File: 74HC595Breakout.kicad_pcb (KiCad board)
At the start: 2 copper layers, 30.7 x 33.5 mm, 12 parts, among them J1 Input, J2 Chain, J3 Output, U1 74HC595, U2 ULN2803A

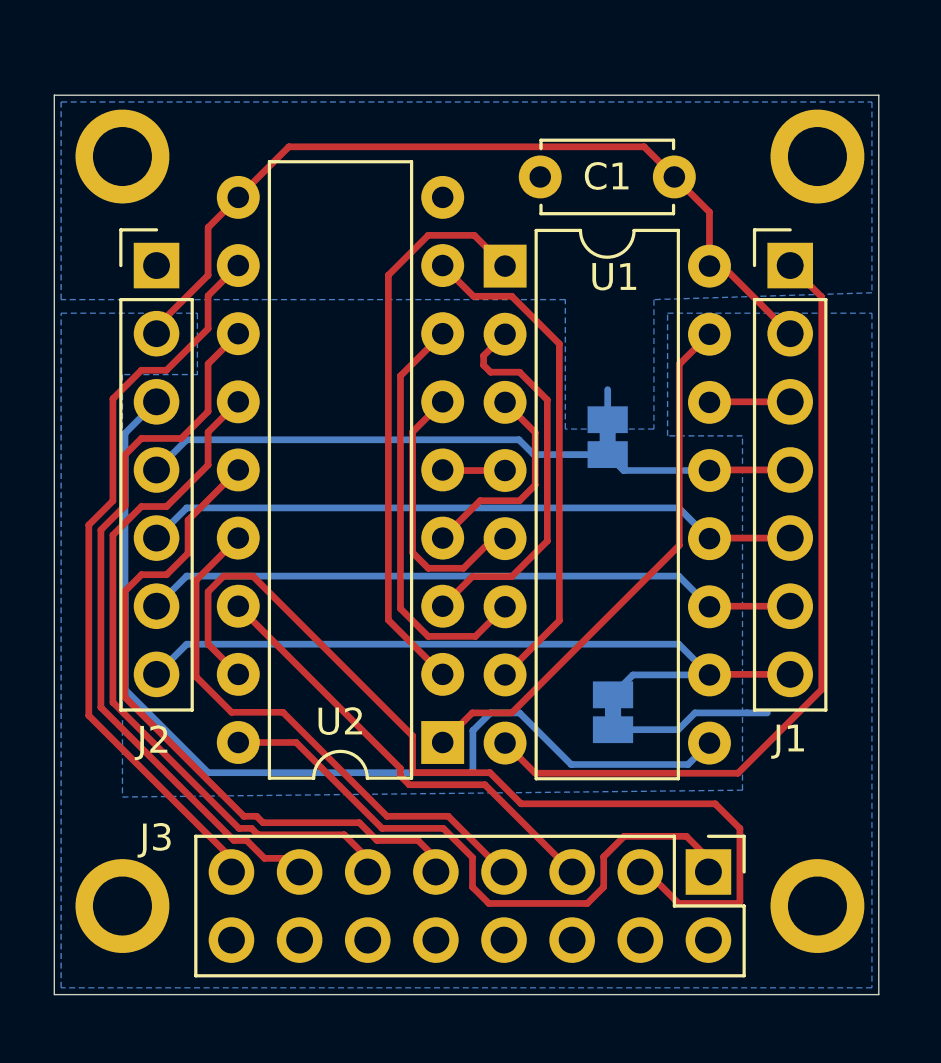
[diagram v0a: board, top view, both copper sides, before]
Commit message: Update for inductive isolation and higher current capacity.
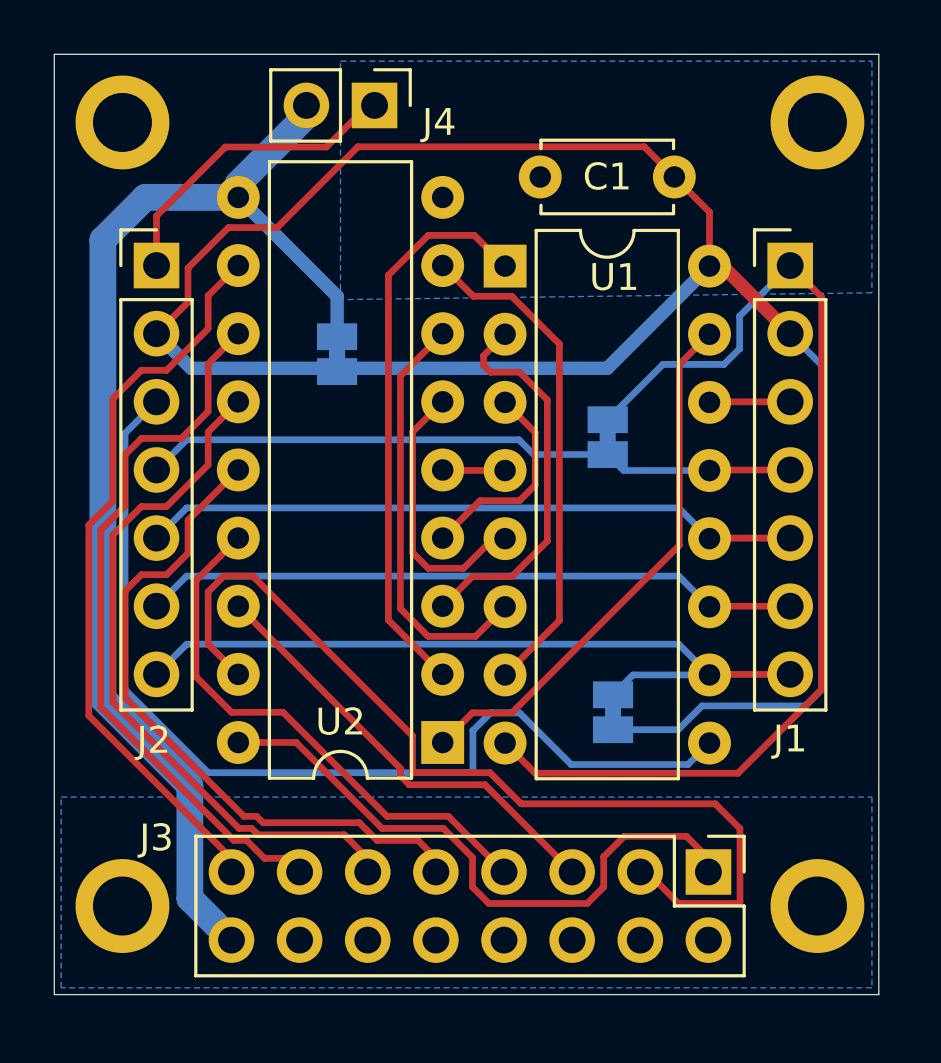
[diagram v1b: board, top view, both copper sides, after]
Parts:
- added J4: Load Power, Connector_PinHeader_2.54mm:PinHeader_1x02_P2.54mm_Vertical, F.Cu at (130.8, 76.8)
- added JP3: Power Select, Jumper:SolderJumper-2_P1.3mm_Bridged_Pad1.0x1.5mm, B.Cu at (129.4, 86.1)
- moved REF** 1.27 mm to (147.3, 77.5)
- moved REF** 1.27 mm to (121.4, 77.5)
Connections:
- J3 pad 10: VCC -> Vdrive
- J3 pad 11: VCC -> Vdrive
- J3 pad 12: VCC -> Vdrive
- J3 pad 13: VCC -> Vdrive
- J3 pad 14: VCC -> Vdrive
- J3 pad 15: VCC -> Vdrive
- J3 pad 16: VCC -> Vdrive
- J3 pad 9: VCC -> Vdrive
- U2 pad 10: VCC -> Vdrive
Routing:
- net Vdrive: track 0.00 -> 45.1 mm
- net VCC: track 37.8 -> 76.5 mm
- net GND: track 31.0 -> 51.4 mm
- added copper zone on B.Cu, net Vdrive
- removed copper zone on B.Cu, net VCC
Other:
- board size 30.7 x 33.5 mm -> 30.7 x 35.1 mm

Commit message: Update with wider traces for power and crowded but informative labels.
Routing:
- net VCC: track 76.5 -> 77.2 mm
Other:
- board text added: "1"
- board text added: "2"
- board text added: "3"
- board text added: "4"
- board text added: "5"
- board text added: "6"
- board text added: "7"
- board text added: "8"
- board text added: "DS"
- board text added: "GND"
- board text added: "Input"
- board text added: "OE"
- board text added: "Output"
- board text added: "RCLK"
- board text added: "SRCLK"
- board text added: "SRCLR"
- board text added: "VCC"
- board text added: "VDrive"
- board text added: "VDrive / GND"
- board text added: "VDrive | VCC"
